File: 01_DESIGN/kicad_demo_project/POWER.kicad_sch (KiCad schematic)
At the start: 18 parts, among them J1 JP2, U2 TPS7A4533DCQR, U8 LM2596S-5

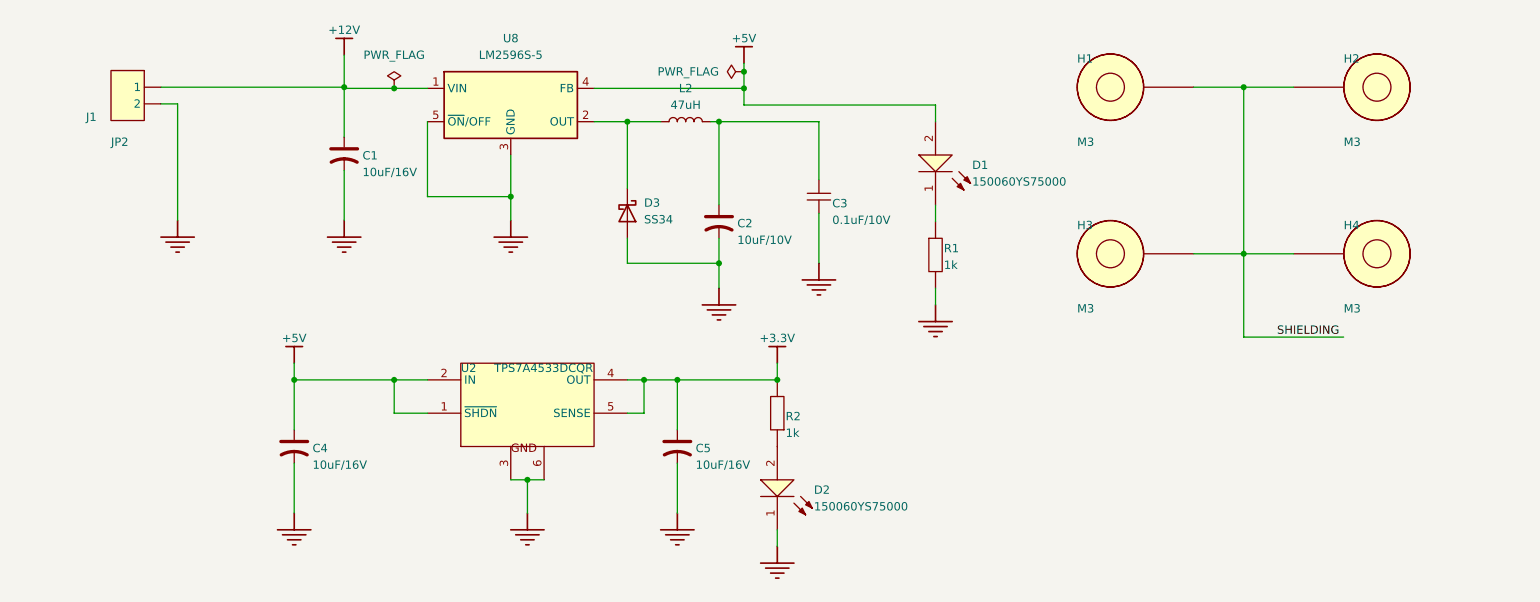
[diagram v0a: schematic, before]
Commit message: Update schematic, PCB
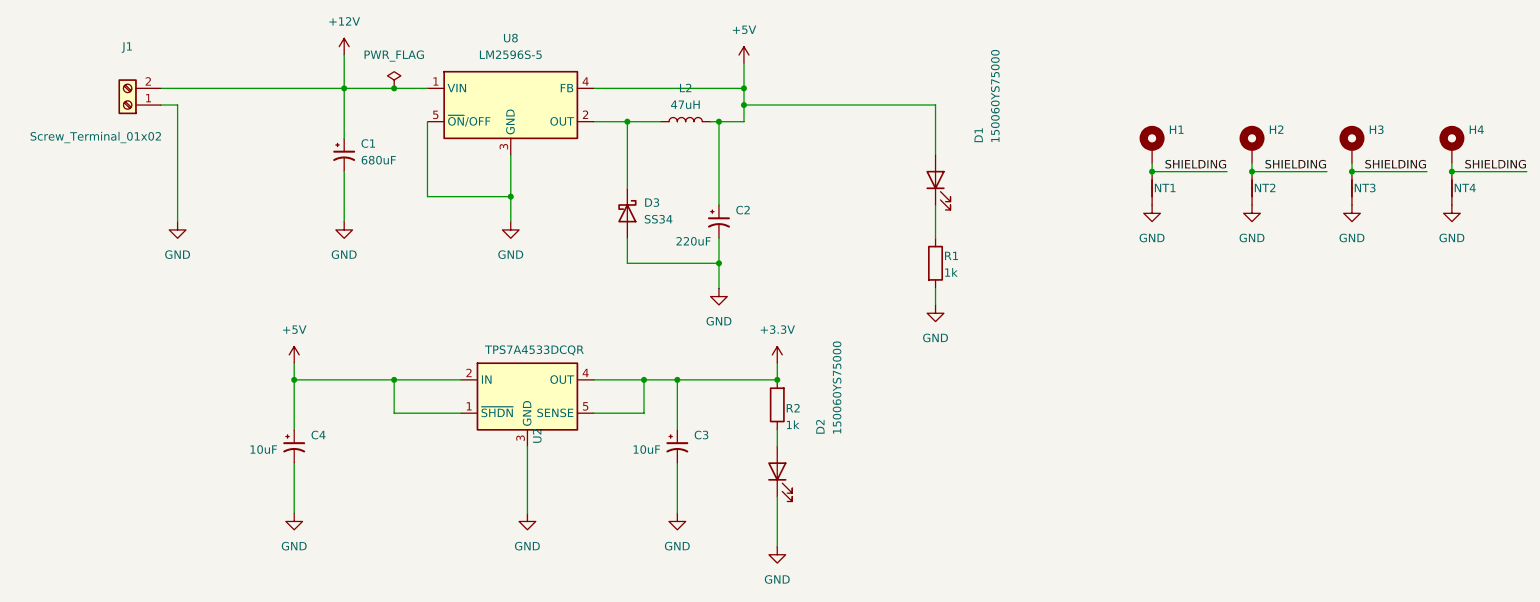
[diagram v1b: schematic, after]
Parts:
- removed C1, C4, C5: 10uF/16V, CAP_MP_2012X170, symbol LABLIB:root_3_CAP_TH_LABLIB.SchLib_0
- removed C2: 10uF/10V, CAP_MP_2012X170, symbol LABLIB:root_3_CAP_TH_LABLIB.SchLib_0
- removed C3: 0.1uF/10V, CAP_C_1608X80, symbol LABLIB:root_3_CAP_SMD_LABLIB.SchLib
- removed H1, H3: M3, HEX-M3, symbol hex_M3:root_0_mirrored_HEX-M3_hex_M3.IntLib
- removed H2, H4: M3, HEX-M3, symbol hex_M3:root_0_HEX-M3_hex_M3.IntLib
- removed J1: JP2, Connector_PinHeader_2.54mm:PinHeader_1x02_P2.54mm_Horizontal, symbol TechMT.VN_Lib:root_0_mirrored_JP2_TechMT.VN_Lib.IntLib
- added C1: 680uF, Capacitor_SMD:CP_Elec_10x10.5, symbol Device:C_Polarized_Small_US
- added C2: 220uF, Capacitor_SMD:CP_Elec_10x10.5, symbol Device:C_Polarized_Small_US
- added C3, C4: 10uF, Capacitor_SMD:C_0805_2012Metric, symbol Device:C_Polarized_Small_US
- added H1, H2, H3, H4: MountingHole_Pad, MountingHole:MountingHole_2.7mm_M2.5_Pad, symbol Mechanical:MountingHole_Pad
- added J1: Screw_Terminal_01x02, TerminalBlock_Phoenix:TerminalBlock_Phoenix_PT-1,5-2-5.0-H_1x02_P5.00mm_Horizontal, symbol Connector:Screw_Terminal_01x02
- added NT1, NT2, NT3, NT4: NetTie_2, NetTie:NetTie-2_SMD_Pad0.5mm, symbol Device:NetTie_2
- D1, D2: symbol Altium Content Vault:root_3_LED_Yellow_2A-1K_Altium Content Vault -> Device:LED
- R1: footprint RES_C_1608X60 -> Resistor_SMD:R_0603_1608Metric; symbol Altium_Lib_by_KhueNguyenCreator:root_3_Tro 0603 1% 10k_Altium_Lib_by_KhueNguyenCreator.IntLib -> Device:R
- R2: footprint RES_C_1608X60 -> Resistor_SMD:R_0603_1608Metric; symbol Altium_Lib_by_KhueNguyenCreator:root_1_Tro 0603 1% 10k_Altium_Lib_by_KhueNguyenCreator.IntLib -> Device:R
- U2: footprint Package_TO_SOT_SMD:SOT-223-6 -> Package_TO_SOT_SMD:TO-263-5_TabPin3; symbol Altium Content Vault:root_0_TI-TXXXXAXXXDCQ_KTTX_Altium Content Vault -> Regulator_Linear:TPS7A45xxKTT
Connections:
- net +12V: now also C1.1, J1.2 (Pin_2)
- net +3.3V: now also C3.1
- net +5V: now also L2.2, C2.1, C4.1
- net GND: now also C1.2, C2.2, C3.2, C4.2, J1.1 (Pin_1), NT1.1, NT2.1, NT3.1, NT4.1; no longer U2.6 (GND)
- net SHIELDING: now also H1.1, H2.1, H3.1, H4.1, NT1.2, NT2.2, NT3.2, NT4.2
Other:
- moved on the sheet: R1, R2
